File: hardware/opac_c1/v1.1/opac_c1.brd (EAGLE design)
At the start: 49 x 90.9 mm, 68 parts, among them IC2 CP2102, IC3 ATSHA204_SOIC8, IC4 MP1584, IC5 TSC2046QFN, IC6 ATMega-328, IC7 RT9300, IC8 DS1307SO8, Q1 MMBT2222A, Q2 32.768kHz mc306, SW1 PROG, X1 8 MHz

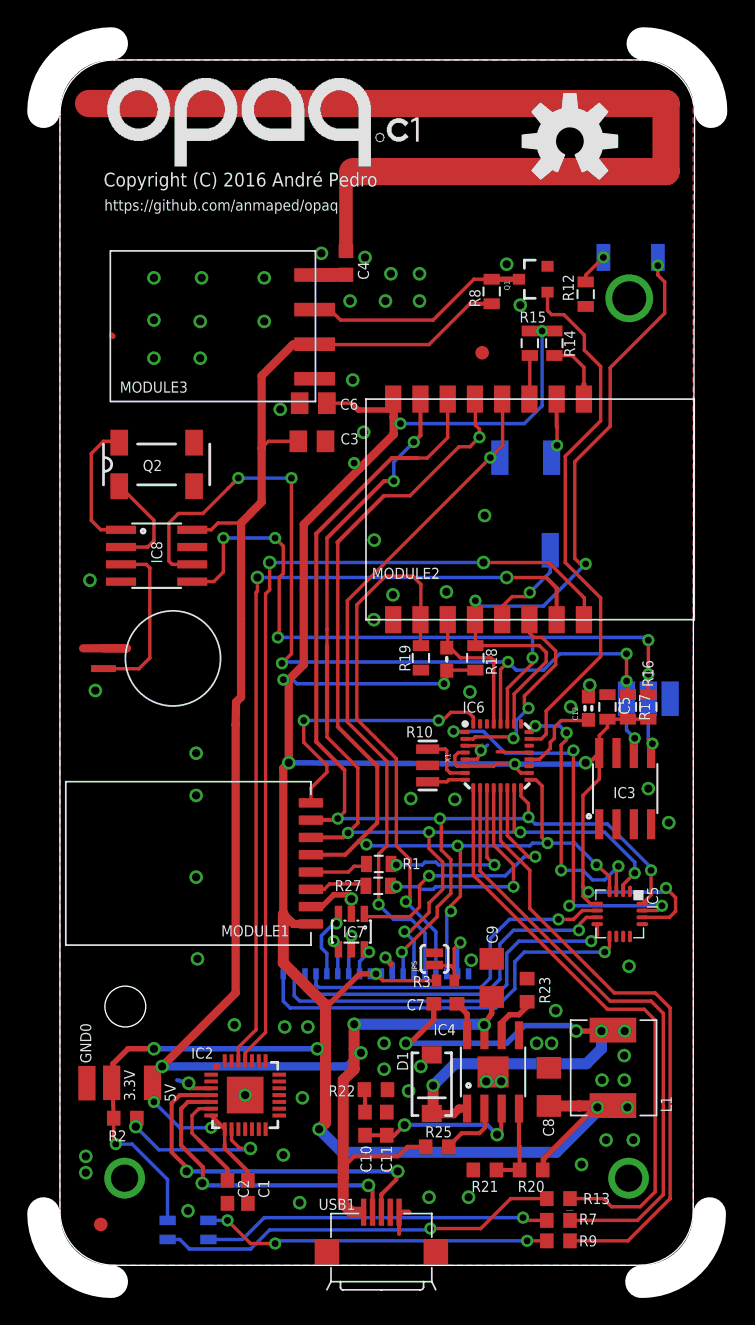
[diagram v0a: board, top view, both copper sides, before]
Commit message: Several issues of the Opaq c1 hardware have been fixed.
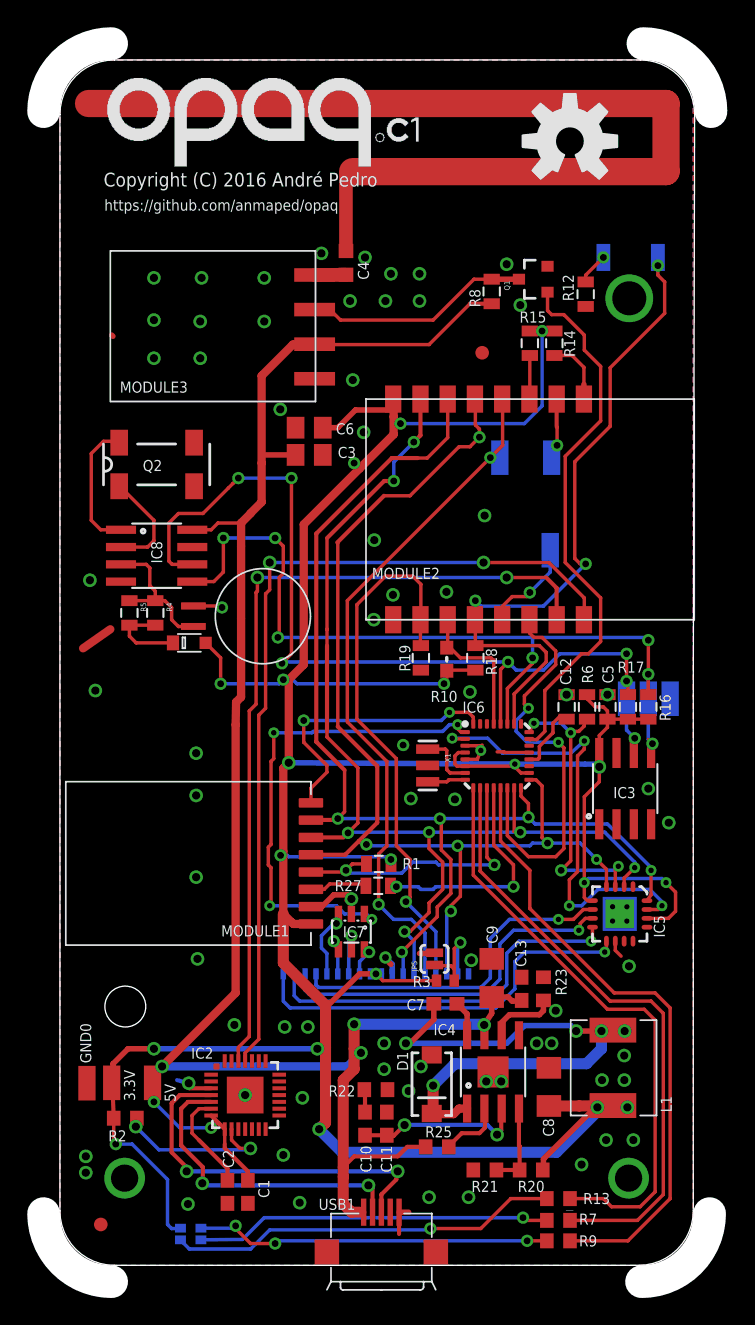
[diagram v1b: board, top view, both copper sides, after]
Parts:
- added C13: (no value), resistor:C0603
- added R4, R5, R6: (no value), resistor:0805
- added U$2: DB2J31400L, apedro_lib:SMINI2-F5-B
- C12: device LowPowerLab:0603-CAP -> SparkFun-Passives:0805
- IC5: device TSC2046:QFN16 -> TSC2046:QFN16-4X4
- R12: value (none) -> 1k
- R14, R15, R18: value (none) -> 4k7
- U$4: value LED-TRICOLOR -> RGBLED; device SparkFun-LED:LED-TRICOLOR-SMD -> apedro_lib:RGBLED0603
- moved U$3 7.29 mm to (14.9, 47.7)
- moved C6 1.82 mm to (18.3, 61.5)
- moved C12 1.60 mm to (37.2, 41.0)
- moved R23 1.20 mm to (35.5, 20.3)
- moved C3 1.02 mm to (18.3, 59.5)
- moved U$4 0.36 mm to (9.60, 2.30), turned to 180 degrees
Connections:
- net 3.3V: now also R1.1, R6.1, U$2.P$2, U$4.P$3; no longer U$4.A
- net AVR_CS: now also IC6.14; no longer IC6.2
- net GND: now also C13.2
- net N$1: now also R4.1, R5.1
- net N$14: now also U$4.P$2; no longer U$4.G
- net N$20: now also U$4.P$4; no longer U$4.B
- net N$3: now also R4.2, R5.2, U$2.P$1; no longer MODULE1.4, R1.2
- net N$7: now also U$4.P$1; no longer U$4.R
- net NRF24_CSN: now also MODULE1.4, R1.2; no longer R1.1
- net TFT_DIM: now also IC6.1; no longer IC6.14
- net TOUCH_CS: now also R6.2
- net TOUCH_IRQ: now also IC6.2; no longer IC6.1
- net VCC: now also C13.1
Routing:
- net 3.3V: track 240.6 -> 262.8 mm, vias 17 -> 20
- net AVR_CS: track 15.0 -> 30.7 mm
- net TFT_DIM: track 21.6 -> 36.7 mm, vias 2 -> 4
- net NRF24_CSN: track 13.7 -> 21.6 mm
- net TOUCH_IRQ: track 30.3 -> 33.2 mm
- net VCC: track 147.0 -> 149.5 mm
- net GND: track 22.7 -> 24.6 mm, vias 71 -> 73
- net TOUCH_CS: track 20.2 -> 22.0 mm
- net N$1: track 12.6 -> 10.8 mm
- net N$3: track 4.39 -> 6.11 mm
- net N$33: track 3.64 -> 5.12 mm
- net AREF: track 6.28 -> 5.22 mm
- net N$7: track 29.7 -> 28.8 mm
- net RST: track 11.5 -> 12.2 mm
- net N$20: track 25.6 -> 26.2 mm
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
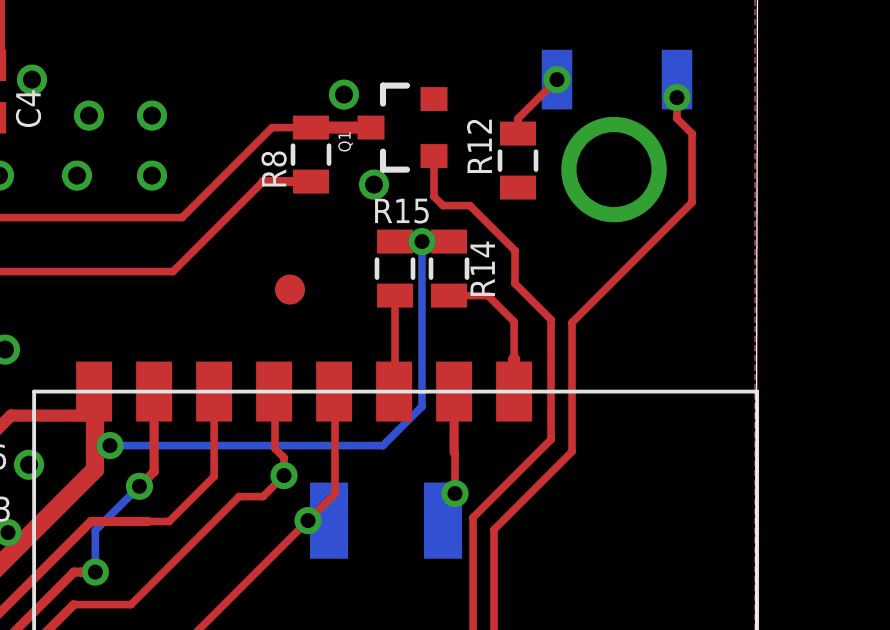
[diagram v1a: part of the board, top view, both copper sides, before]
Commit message: Opaq c1 hardware has been updated.
- pull-up resistor have been added to RF433 signal.
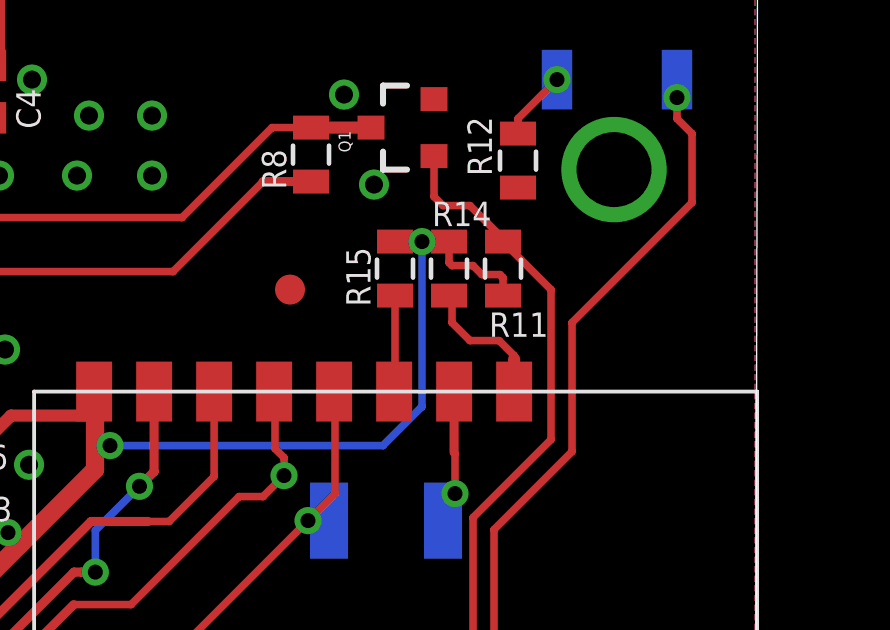
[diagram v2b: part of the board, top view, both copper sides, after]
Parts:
- added R11: (no value), resistor:0805
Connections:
- net 3.3V: now also R11.1
- net SIGNAL433: now also R11.2
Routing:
- net 3.3V: track 262.8 -> 266.2 mm
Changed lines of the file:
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@@
 </element>
 <element name="R14" library="resistor" package="0805" value="4k7" x="36.3" y="67.7" smashed="yes" rot="R270">
-<attribute name="NAME" x="37.016" y="68.662" size="0.8128" layer="25" ratio="14" rot="R270"/>
+<attribute name="NAME" x="35.738" y="69.116" size="0.8128" layer="25" ratio="14"/>
 <attribute name="VALUE" x="34.014" y="68.462" size="1.27" layer="27" rot="R270"/>
 </element>
 <element name="R15" library="resistor" package="0805" value="4k7" x="34.5" y="67.7" smashed="yes" rot="R270">
-<attribute name="NAME" x="33.738" y="69.216" size="0.8128" layer="25" ratio="14"/>
+<attribute name="NAME" x="33.684" y="66.438" size="0.8128" layer="25" ratio="14" rot="R90"/>
 <attribute name="VALUE" x="32.214" y="68.462" size="1.27" layer="27" rot="R270"/>
 </element>
@@
 <attribute name="NAME" x="38.3255" y="44.062" size="0.8128" layer="25" ratio="14" rot="R270"/>
 <attribute name="VALUE" x="37.303" y="42.016" size="0.4064" layer="27" rot="R270"/>
+</element>
+<element name="R11" library="resistor" package="0805" value="" x="38.1" y="67.7" smashed="yes" rot="R90">
+<attribute name="NAME" x="37.638" y="65.4255" size="0.8128" layer="25" ratio="14"/>
+<attribute name="VALUE" x="39.497" y="66.684" size="0.4064" layer="27" rot="R90"/>
 </element>
 </elements>
@@
 <wire x1="39.9" y1="41" x2="40.2" y2="40.7" width="0.254" layer="1"/>
 <wire x1="40.2" y1="40.7" x2="40.2" y2="40.1" width="0.254" layer="1"/>
+<contactref element="R11" pad="1"/>
+<wire x1="36.3" y1="68.6" x2="36.3" y2="67.9" width="0.254" layer="1"/>
+<wire x1="36.3" y1="67.9" x2="36.4" y2="67.8" width="0.254" layer="1"/>
+<wire x1="36.4" y1="67.8" x2="37.1" y2="67.8" width="0.254" layer="1"/>
+<wire x1="37.1" y1="67.8" x2="37.4" y2="67.5" width="0.254" layer="1"/>
+<wire x1="37.4" y1="67.5" x2="38" y2="67.5" width="0.254" layer="1"/>
+<wire x1="38" y1="67.5" x2="38.1" y2="67.4" width="0.254" layer="1"/>
+<wire x1="38.1" y1="67.4" x2="38.1" y2="66.8" width="0.254" layer="1"/>
 <wire x1="23.2" y1="21.4" x2="22.8" y2="21.4" width="0" layer="19" extent="16-16"/>
 </signal>
@@
 <contactref element="IC6" pad="23"/>
 <wire x1="39.7" y1="45.8" x2="39.7" y2="49" width="0.254" layer="1"/>
-<wire x1="39.7" y1="62" x2="39.7" y2="66" width="0.254" layer="1"/>
+<wire x1="39.7" y1="62" x2="39.7" y2="67" width="0.254" layer="1"/>
 <wire x1="39.7" y1="49" x2="37.1" y2="51.6" width="0.254" layer="1"/>
 <wire x1="37.1" y1="51.6" x2="37.1" y2="59.4" width="0.254" layer="1"/>
 <wire x1="37.1" y1="59.4" x2="39.7" y2="62" width="0.254" layer="1"/>
-<wire x1="39.7" y1="66" x2="38.5" y2="67.2" width="0.254" layer="1"/>
-<wire x1="38.5" y1="67.2" x2="38.5" y2="68.3" width="0.254" layer="1"/>
-<wire x1="38.5" y1="68.3" x2="37" y2="69.8" width="0.254" layer="1"/>
 <wire x1="37" y1="69.8" x2="36.1" y2="69.8" width="0.254" layer="1"/>
 <wire x1="36.1" y1="69.8" x2="35.8" y2="70.1" width="0.254" layer="1"/>
@@
 <wire x1="38.3" y1="44.9" x2="38.8" y2="44.9" width="0.254" layer="1"/>
 <wire x1="38.8" y1="44.9" x2="39.7" y2="45.8" width="0.254" layer="1"/>
+<contactref element="R11" pad="2"/>
+<wire x1="39.7" y1="67" x2="38.1" y2="68.6" width="0.254" layer="1"/>
+<wire x1="38.1" y1="68.6" x2="38.1" y2="68.7" width="0.254" layer="1"/>
+<wire x1="38.1" y1="68.7" x2="37" y2="69.8" width="0.254" layer="1"/>
 </signal>
 <signal name="N$11">
@@
 <contactref element="R14" pad="2"/>
 <wire x1="38.47" y1="64.68" x2="38.47" y2="63.6" width="0.4064" layer="1"/>
-<wire x1="38.47" y1="64.68" x2="38.47" y2="65.93" width="0.254" layer="1"/>
-<wire x1="38.47" y1="65.93" x2="37.6" y2="66.8" width="0.254" layer="1"/>
-<wire x1="37.6" y1="66.8" x2="36.3" y2="66.8" width="0.254" layer="1"/>
+<wire x1="38.47" y1="64.68" x2="38.47" y2="64.8" width="0.254" layer="1"/>
+<wire x1="36.3" y1="66.8" x2="36.4" y2="66.8" width="0.254" layer="1"/>
+<wire x1="36.4" y1="66.8" x2="36.4" y2="65.9" width="0.254" layer="1"/>
+<wire x1="36.4" y1="65.9" x2="37" y2="65.3" width="0.254" layer="1"/>
+<wire x1="37" y1="65.3" x2="37.97" y2="65.3" width="0.254" layer="1"/>
+<wire x1="37.97" y1="65.3" x2="38.47" y2="64.8" width="0.254" layer="1"/>
 </signal>
 <signal name="N$28">

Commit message: Added the new fixes for opaq c1 hardware.
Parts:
- added ADC6: TPTP09R, testpad:TP09R
- added RX, TX: TPTP10SQ, testpad:TP10SQ
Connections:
- net A6: now also ADC6.TP
- net D0_RX: now also RX.TP
- net D1_TX: now also TX.TP
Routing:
- net D1_TX: track 0.00 -> 9.04 mm
- net D0_RX: track 0.00 -> 7.58 mm
- net A6: track 0.00 -> 1.69 mm
- net TOUCH_IRQ: track 33.2 -> 33.8 mm

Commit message: Updated version of the opaq c1 hardware.
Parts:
- C10, C13, C7: value (none) -> 0.1uf
- C4: value (none) -> 47nH
- C8, C9: value (none) -> 10uf
- D1: value (none) -> SS34
- L1: value (none) -> 4.7uh
- R20: value (none) -> 8.2k
- R21: value (none) -> 24k
- R22, R23, R25: value (none) -> 100k
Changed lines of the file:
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@@
 <attribute name="VALUE" x="37.489" y="6.932" size="1.27" layer="27" rot="R180"/>
 </element>
-<element name="C4" library="resistor" package="C0603K" value="" x="21" y="73.6" smashed="yes" rot="R90">
+<element name="C4" library="resistor" package="C0603K" value="47nH" x="21" y="73.6" smashed="yes" rot="R90">
 <attribute name="NAME" x="21.875" y="73.7" size="0.8128" layer="25" rot="R270"/>
 <attribute name="VALUE" x="22.9" y="72.6" size="1.016" layer="27" rot="R90"/>
@@
 <attribute name="NAME" x="27.43" y="16.9" size="0.8128" layer="25" ratio="14"/>
 </element>
-<element name="D1" library="SparkFun" package="SMA-DIODE" value="" x="27.3" y="13.3" smashed="yes" rot="R270">
+<element name="D1" library="SparkFun" package="SMA-DIODE" value="SS34" x="27.3" y="13.3" smashed="yes" rot="R270">
 <attribute name="NAME" x="24.751" y="15.686" size="0.8128" layer="25" ratio="14" rot="R270"/>
 <attribute name="VALUE" x="28.951" y="13.046" size="0.4064" layer="27" rot="R270"/>
 </element>
-<element name="L1" library="RNH_IHLP-2525CZ-01" package="2525" value="" x="40.6" y="14.5" smashed="yes" rot="R270">
+<element name="L1" library="RNH_IHLP-2525CZ-01" package="2525" value="4.7uh" x="40.6" y="14.5" smashed="yes" rot="R270">
 <attribute name="NAME" x="44.11" y="12.4322" size="0.8128" layer="25" ratio="14" rot="R270"/>
 <attribute name="VALUE" x="35.52" y="18.31" size="1.27" layer="27" rot="R270"/>
 </element>
-<element name="C7" library="resistor" package="C0603" value="" x="28.3" y="19.2" smashed="yes" rot="R180">
+<element name="C7" library="resistor" package="C0603" value="0.1uf" x="28.3" y="19.2" smashed="yes" rot="R180">
 <attribute name="NAME" x="26.789" y="19.538" size="0.8128" layer="25" ratio="14" rot="R180"/>
 <attribute name="VALUE" x="29.189" y="21.232" size="1.27" layer="27" rot="R180"/>
 </element>
-<element name="C8" library="resistor" package="C3216" value="" x="35.9" y="13.1" smashed="yes" rot="R90">
+<element name="C8" library="resistor" package="C3216" value="10uf" x="35.9" y="13.1" smashed="yes" rot="R90">
 <attribute name="NAME" x="35.462" y="10.789" size="0.8128" layer="25" ratio="14" rot="R270"/>
 <attribute name="VALUE" x="37.932" y="12.211" size="1.27" layer="27" rot="R90"/>
 </element>
-<element name="R20" library="resistor" package="R0603" value="" x="34.6" y="7" smashed="yes">
+<element name="R20" library="resistor" package="R0603" value="8.2k" x="34.6" y="7" smashed="yes">
 <attribute name="NAME" x="33.611" y="5.389" size="0.8128" layer="25" ratio="14"/>
 <attribute name="VALUE" x="33.711" y="4.968" size="1.27" layer="27"/>
 </element>
-<element name="R21" library="resistor" package="R0603" value="" x="31.2" y="7" smashed="yes">
+<element name="R21" library="resistor" package="R0603" value="24k" x="31.2" y="7" smashed="yes">
 <attribute name="NAME" x="30.211" y="5.389" size="0.8128" layer="25" ratio="14"/>
 <attribute name="VALUE" x="30.311" y="4.968" size="1.27" layer="27"/>
 </element>
-<element name="C9" library="resistor" package="C3216" value="" x="31.7" y="21.1" smashed="yes" rot="R90">
+<element name="C9" library="resistor" package="C3216" value="10uf" x="31.7" y="21.1" smashed="yes" rot="R90">
 <attribute name="NAME" x="32.138" y="23.611" size="0.8128" layer="25" ratio="14" rot="R90"/>
 <attribute name="VALUE" x="33.732" y="20.211" size="1.27" layer="27" rot="R90"/>
 </element>
-<element name="C10" library="resistor" package="C0603" value="" x="22.4" y="10.4" smashed="yes" rot="R90">
+<element name="C10" library="resistor" package="C0603" value="0.1uf" x="22.4" y="10.4" smashed="yes" rot="R90">
 <attribute name="NAME" x="22.062" y="8.789" size="0.8128" layer="25" ratio="14" rot="R270"/>
 <attribute name="VALUE" x="24.432" y="9.511" size="1.27" layer="27" rot="R90"/>
@@
 <attribute name="VALUE" x="26.032" y="9.511" size="1.27" layer="27" rot="R90"/>
 </element>
-<element name="R22" library="resistor" package="R0603" value="" x="23.2" y="12.9" smashed="yes" rot="R180">
+<element name="R22" library="resistor" package="R0603" value="100k" x="23.2" y="12.9" smashed="yes" rot="R180">
 <attribute name="NAME" x="21.689" y="13.211" size="0.8128" layer="25" ratio="14" rot="R180"/>
 <attribute name="VALUE" x="24.089" y="14.932" size="1.27" layer="27" rot="R180"/>
 </element>
-<element name="R23" library="resistor" package="R0603" value="" x="35.5" y="20.3" smashed="yes" rot="R270">
+<element name="R23" library="resistor" package="R0603" value="100k" x="35.5" y="20.3" smashed="yes" rot="R270">
 <attribute name="NAME" x="36.389" y="21.789" size="0.8128" layer="25" ratio="14" rot="R270"/>
 <attribute name="VALUE" x="33.468" y="21.189" size="1.27" layer="27" rot="R270"/>
 </element>
-<element name="R25" library="resistor" package="R0603" value="" x="27.7" y="8.7" smashed="yes" rot="R180">
+<element name="R25" library="resistor" package="R0603" value="100k" x="27.7" y="8.7" smashed="yes" rot="R180">
 <attribute name="NAME" x="28.789" y="10.211" size="0.8128" layer="25" ratio="14" rot="R180"/>
 <attribute name="VALUE" x="28.589" y="10.732" size="1.27" layer="27" rot="R180"/>
@@
 <attribute name="NAME" x="35.6" y="54" size="0.8128" layer="26" ratio="14" rot="MR90"/>
 </element>
-<element name="C13" library="resistor" package="C0603" value="" x="33.9" y="20.3" smashed="yes" rot="R90">
+<element name="C13" library="resistor" package="C0603" value="0.1uf" x="33.9" y="20.3" smashed="yes" rot="R90">
 <attribute name="NAME" x="34.238" y="21.911" size="0.8128" layer="25" ratio="14" rot="R90"/>
 <attribute name="VALUE" x="35.932" y="19.411" size="1.27" layer="27" rot="R90"/>
